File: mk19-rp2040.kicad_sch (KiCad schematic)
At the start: 145 parts, among them J1 USB_C_Receptacle_USB2.0, J10 Conn_01x02, J11 Conn_01x03_Socket, J12 USB_C_Receptacle_USB2.0, J13 USB_C_Receptacle_USB2.0, J2 Conn_01x03_Socket, J3 Conn_01x02_Socket, J4 Conn_01x06_Socket, J5 Conn_01x02, J7 Conn_01x02_Socket, J8 Conn_01x02_Socket, J9 Conn_01x02_Socket, T1 Conn_01x01_Socket, T10 Conn_01x01_Socket, T11 Conn_01x01_Socket, T12 Conn_01x01_Socket, T13 Conn_01x01_Socket, T14 Conn_01x01_Socket, T15 Conn_01x01_Socket, T2 Conn_01x01_Socket, T3 Conn_01x01_Socket, T5 Conn_01x01_Socket, T6 Conn_01x01_Socket, T7 Conn_01x01_Socket, T9 Conn_01x01_Socket, U1 RP2040, U10 1N4148W_C81598, U11 1N4148W_C81598, U12 1N4148W_C81598, U13 1N4148W_C81598, U14 1N4148W_C81598, U15 1N4148W_C81598, U16 W25Q128JVSIQTR, U3 XC6210B332MR-G, U6 8_01A0_008200, U7 8_01A0_008200, U9 1N4148W_C81598, Y1 Crystal_GND24

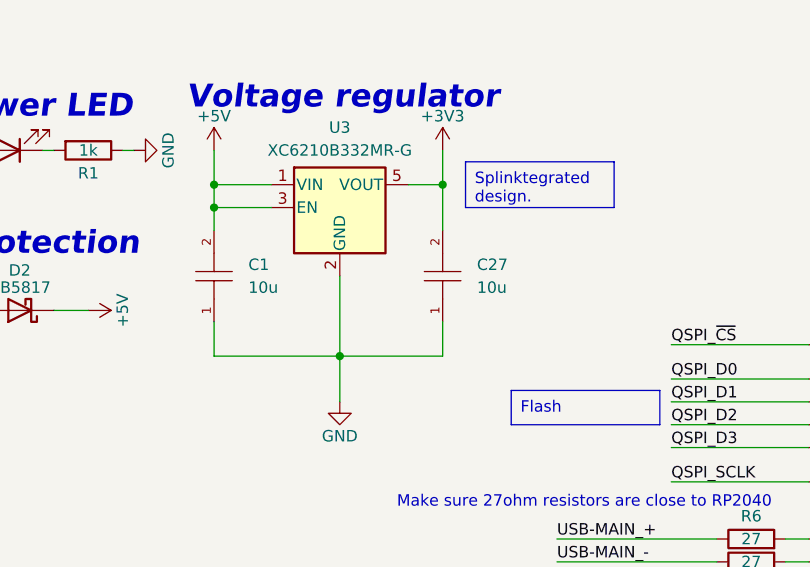
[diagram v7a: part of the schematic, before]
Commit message: reworking the voltage regulator capacitors
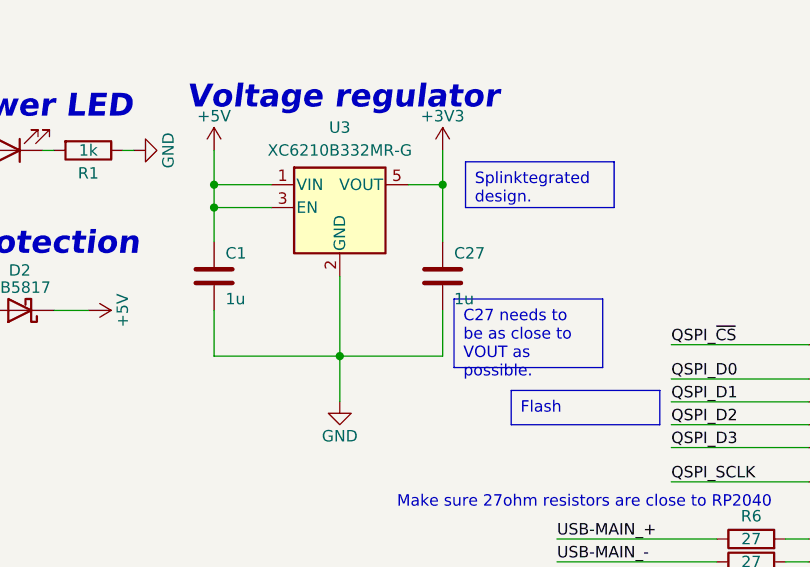
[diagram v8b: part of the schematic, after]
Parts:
- removed C1, C27: 10u, ct-kicad:C0805, symbol ct-kicad:GRM21BR61H106KE43L
- added C1, C27: 1u, ct-kicad:C0402, symbol Device:C
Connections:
- net +3V3: now also C27.1
- net +5V: now also C1.1
- net GND: now also C1.2, C27.2
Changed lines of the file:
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@@
 	(wire
 		(pts
-			(xy 391.16 63.5) (xy 391.16 67.31)
-		)
-		(stroke
-			(width 0)
-			(type default)
-		)
-	)
-	(wire
-		(pts
 			(xy 160.02 431.8) (xy 185.42 431.8)
 		)
@@
 	(wire
 		(pts
+			(xy 391.16 62.23) (xy 391.16 67.31)
+		)
+		(stroke
+			(width 0)
+			(type default)
+		)
+	)
+	(wire
+		(pts
 			(xy 467.36 44.45) (xy 469.9 44.45)
 		)
@@
 	(wire
 		(pts
-			(xy 365.76 67.31) (xy 365.76 63.5)
-		)
-		(stroke
-			(width 0)
-			(type default)
-		)
-	)
-	(wire
-		(pts
 			(xy 535.94 289.56) (xy 525.78 289.56)
 		)
@@
 	(wire
 		(pts
+			(xy 365.76 62.23) (xy 365.76 67.31)
+		)
+		(stroke
+			(width 0)
+			(type default)
+		)
+	)
+	(wire
+		(pts
 			(xy 457.2 44.45) (xy 457.2 46.99)
 		)
@@
 	(wire
 		(pts
-			(xy 391.16 48.26) (xy 391.16 53.34)
+			(xy 391.16 48.26) (xy 391.16 54.61)
 		)
 		(stroke
@@
 	(wire
 		(pts
-			(xy 365.76 50.8) (xy 365.76 53.34)
-		)
-		(stroke
-			(width 0)
-			(type default)
-		)
-	)
-	(wire
-		(pts
 			(xy 561.34 39.37) (xy 561.34 36.83)
 		)
@@
 	(wire
 		(pts
+			(xy 365.76 50.8) (xy 365.76 54.61)
+		)
+		(stroke
+			(width 0)
+			(type default)
+		)
+	)
+	(wire
+		(pts
 			(xy 91.44 74.93) (xy 90.17 74.93)
 		)
@@
 		)
 	)
+	(text_box "C27 needs to be as close to VOUT as possible."
+		(exclude_from_sim no)
+		(at 392.43 60.96 0)
+		(size 16.51 7.62)
+		(stroke
+			(width 0)
+			(type default)
+		)
+		(fill
+			(type none)
+		)
+		(effects
+			(font
+				(face "Futura")
+				(size 1.27 1.27)
+			)
+			(justify left top)
+		)
+	)
 	(text_box "For edge rails, as per JLC."
 		(exclude_from_sim no)
@@
 	)
 	(symbol
+		(lib_id "Device:C")
+		(at 365.76 58.42 0)
+		(unit 1)
+		(exclude_from_sim no)
+		(in_bom yes)
+		(on_board yes)
+		(dnp no)
+		(property "Reference" "C1"
+			(at 367.03 55.88 0)
+			(effects
+				(font
+					(size 1.27 1.27)
+				)
+				(justify left)
+			)
+		)
+		(property "Value" "1u"
+			(at 367.03 60.96 0)
+			(effects
+				(font
+					(size 1.27 1.27)
+				)
+				(justify left)
+			)
+		)
+		(property "Footprint" "ct-kicad:C0402"
+			(at 366.7252 62.23 0)
+			(effects
+				(font
+					(size 1.27 1.27)
+				)
+				(hide yes)
+			)
+		)
+		(property "Datasheet" "~"
+			(at 365.76 58.42 0)
+			(effects
+				(font
+					(size 1.27 1.27)
+				)
+				(hide yes)
+			)
+		)
+		(property "Description" ""
+			(at 365.76 58.42 0)
+			(effects
+				(font
+					(size 1.27 1.27)
+				)
+				(hide yes)
+			)
+		)
+		(property "LCSC" "C52923"
+			(at 365.76 58.42 0)
+			(effects
+				(font
+					(size 1.27 1.27)
+				)
+				(hide yes)
+			)
+		)
+		(pin "1"
+		)
+		(pin "2"
+		)
+		(instances
+			(project "mk19-rp2040"
+				(path "/7353e96a-343a-4876-b497-b1d205a14d97"
+					(reference "C1")
+					(unit 1)
+				)
+			)
+		)
+	)
+	(symbol
 		(lib_id "ct-kicad:2N7002")
 		(at 113.03 208.28 0)
@@
 	)
 	(symbol
-		(lib_id "ct-kicad:GRM21BR61H106KE43L")
-		(at 365.76 58.42 90)
-		(unit 1)
-		(exclude_from_sim no)
-		(in_bom yes)
-		(on_board yes)
-		(dnp no)
-		(fields_autoplaced yes)
-		(property "Reference" "C1"
-			(at 369.57 57.1499 90)
-			(effects
-				(font
-					(size 1.27 1.27)
-				)
-				(justify right)
-			)
-		)
-		(property "Value" "10u"
-			(at 369.57 59.6899 90)
-			(effects
-				(font
-					(size 1.27 1.27)
-				)
-				(justify right)
-			)
-		)
-		(property "Footprint" "ct-kicad:C0805"
-			(at 375.92 58.42 0)
-			(effects
-				(font
-					(size 1.27 1.27)
-					(italic yes)
-				)
-				(hide yes)
-			)
-		)
-		(property "Datasheet" "https://item.szlcsc.com/373011.html"
-			(at 365.633 60.706 0)
-			(effects
-				(font
-					(size 1.27 1.27)
-				)
-				(justify left)
-				(hide yes)
-			)
-		)
-		(property "Description" ""
-			(at 365.76 58.42 0)
-			(effects
-				(font
-					(size 1.27 1.27)
-				)
-				(hide yes)
-			)
-		)
-		(property "LCSC" "C440198"
-			(at 365.76 58.42 0)
-			(effects
-				(font
-					(size 1.27 1.27)
-				)
-				(hide yes)
-			)
-		)
-		(pin "2"
-		)
-		(pin "1"
-		)
-		(instances
-			(project "mk19-rp2040"
-				(path "/7353e96a-343a-4876-b497-b1d205a14d97"
-					(reference "C1")
-					(unit 1)
-				)
-			)
-		)
-	)
-	(symbol
 		(lib_id "power:GND")
 		(at 203.2 86.36 90)
@@
 	)
 	(symbol
+		(lib_id "Device:C")
+		(at 391.16 58.42 0)
+		(unit 1)
+		(exclude_from_sim no)
+		(in_bom yes)
+		(on_board yes)
+		(dnp no)
+		(property "Reference" "C27"
+			(at 392.43 55.88 0)
+			(effects
+				(font
+					(size 1.27 1.27)
+				)
+				(justify left)
+			)
+		)
+		(property "Value" "1u"
+			(at 392.43 60.96 0)
+			(effects
+				(font
+					(size 1.27 1.27)
+				)
+				(justify left)
+			)
+		)
+		(property "Footprint" "ct-kicad:C0402"
+			(at 392.1252 62.23 0)
+			(effects
+				(font
+					(size 1.27 1.27)
+				)
+				(hide yes)
+			)
+		)
+		(property "Datasheet" "~"
+			(at 391.16 58.42 0)
+			(effects
+				(font
+					(size 1.27 1.27)
+				)
+				(hide yes)
+			)
+		)
+		(property "Description" ""
+			(at 391.16 58.42 0)
+			(effects
+				(font
+					(size 1.27 1.27)
+				)
+				(hide yes)
+			)
+		)
+		(property "LCSC" "C52923"
+			(at 391.16 58.42 0)
+			(effects
+				(font
+					(size 1.27 1.27)
+				)
+				(hide yes)
+			)
+		)
+		(pin "1"
+		)
+		(pin "2"
+		)
+		(instances
+			(project "mk19-rp2040"
+				(path "/7353e96a-343a-4876-b497-b1d205a14d97"
+					(reference "C27")
+					(unit 1)
+				)
+			)
+		)
+	)
+	(symbol
 		(lib_id "ct-kicad:TYPE-C-31-M-14")
 		(at 369.57 302.26 0)
@@
 					(unit 1)
 				)
-			)
-		)
-	)
-	(symbol
-		(lib_id "ct-kicad:GRM21BR61H106KE43L")
-		(at 391.16 58.42 90)
-		(unit 1)
-		(exclude_from_sim no)
-		(in_bom yes)
-		(on_board yes)
-		(dnp no)
-		(fields_autoplaced yes)
-		(property "Reference" "C27"
-			(at 394.97 57.1499 90)
-			(effects
-				(font
-					(size 1.27 1.27)
-				)
-				(justify right)
-			)
-		)
-		(property "Value" "10u"
-			(at 394.97 59.6899 90)
-			(effects
-				(font
-					(size 1.27 1.27)
-				)
-				(justify right)
-			)
-		)
-		(property "Footprint" "ct-kicad:C0805"
-			(at 401.32 58.42 0)
-			(effects
-				(font
-					(size 1.27 1.27)
-					(italic yes)
-				)
-				(hide yes)
-			)
-		)
-		(property "Datasheet" "https://item.szlcsc.com/373011.html"
-			(at 391.033 60.706 0)
-			(effects
-				(font
-					(size 1.27 1.27)
-				)
-				(justify left)
-				(hide yes)
-			)
-		)
-		(property "Description" ""
-			(at 391.16 58.42 0)
-			(effects
-				(font
-					(size 1.27 1.27)
-				)
-				(hide yes)
-			)
-		)
-		(property "LCSC" "C440198"
-			(at 391.16 58.42 0)
-			(effects
-				(font
-					(size 1.27 1.27)
-				)
-				(hide yes)
-			)
-		)
-		(pin "2"
-		)
-		(pin "1"
-		)
-		(instances
-			(project "mk19-rp2040"
-				(path "/7353e96a-343a-4876-b497-b1d205a14d97"
-					(reference "C27")
-					(unit 1)
-				)
